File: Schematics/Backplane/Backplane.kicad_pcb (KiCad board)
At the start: 2 copper layers, 69.5 x 98.5 mm, 21 parts, among them J1 Edge Connector (SLOT 1), J2 Edge Connector (SLOT 2), J3 Edge Connector (SLOT 3), J4 Edge Connector (SLOT 4), J5 Edge Connector (SLOT 5), J6 Conn_01x06_Socket

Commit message: New Backplane
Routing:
- net GND1: track 166.7 -> 270.0 mm
- net 24V_A: track 128.8 -> 207.6 mm, vias 1 -> 4
- net BATT_A: track 114.5 -> 179.0 mm, vias 4 -> 6
- net 3.3V_A: track 101.2 -> 157.0 mm, vias 1 -> 5
- net 3.3V_B: track 125.3 -> 176.5 mm, vias 1 -> 4
- net 5.0V_A: track 119.6 -> 164.0 mm, vias 1 -> 4
- net BATT_B: track 162.5 -> 164.9 mm
- net GND2: track 242.5 -> 240.2 mm
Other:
- board text added: "Backplane PCB Rev 1.1 QRET Mar 2025 Abigail Elms Kennan Bays Owen Price"
- board text removed: "Backplane PCB Rev 1.1 QRET Mar 2025 Kennan Bays Owen Price"

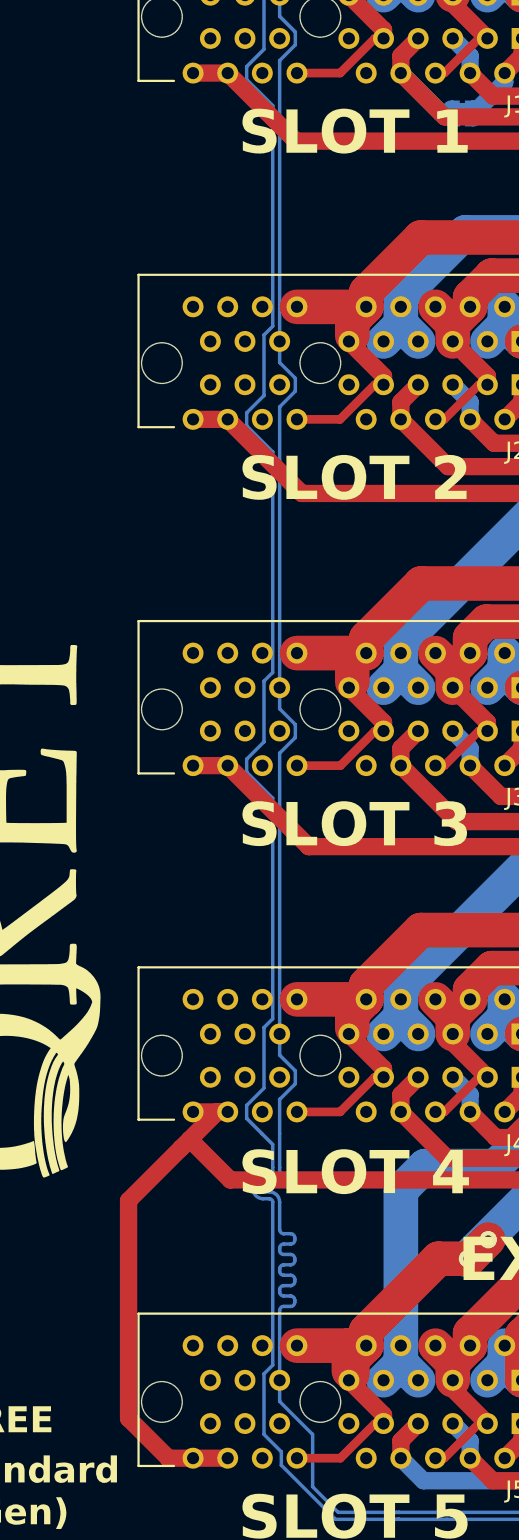
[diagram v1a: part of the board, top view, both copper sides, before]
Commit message: Made Minor Updates
- Update Silk Screen to Reflect 2026 Year
- Connected CAN_P Line to Connectors
- Moved R2 Slightly Away from the Edge
- Fixed DRC Error With J6

Still To Do:
- Name Board
- Update Silkscreen
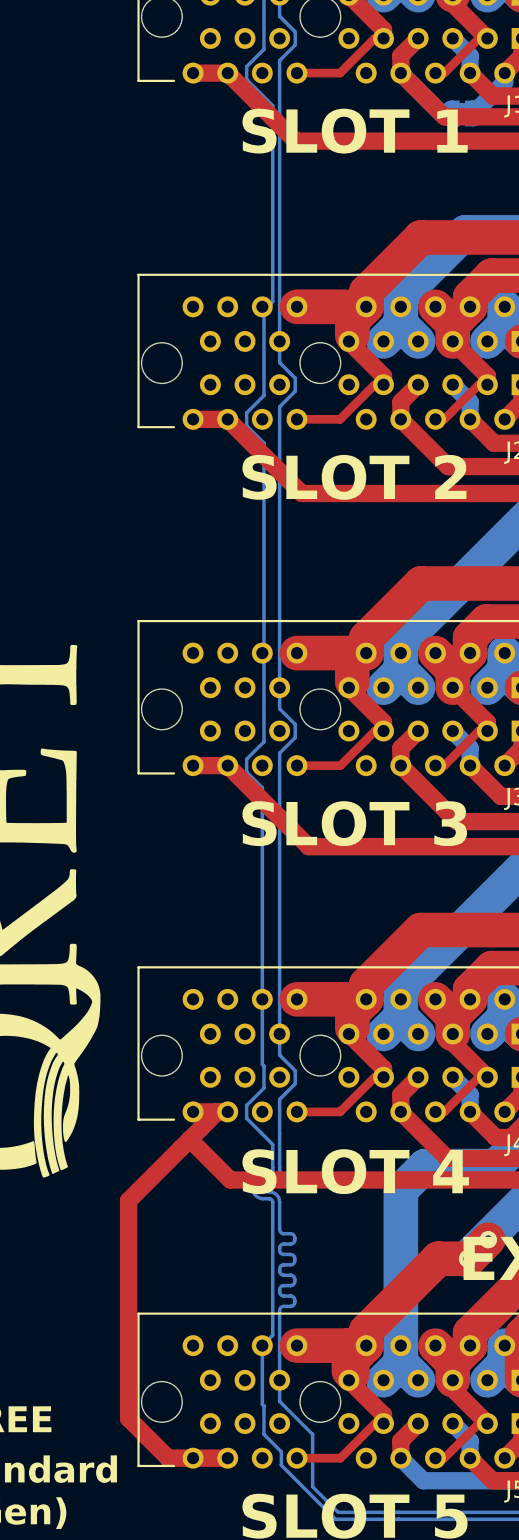
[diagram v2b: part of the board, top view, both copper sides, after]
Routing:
- net CAN_P: track 144.9 -> 144.1 mm
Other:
- board text added: "Backplane PCB Rev 1.2 QRET Mar 2026 Abigail Elms Kennan Bays Owen Price"
- board text removed: "Backplane PCB Rev 1.1 QRET Mar 2025 Abigail Elms Kennan Bays Owen Price"
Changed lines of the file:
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@@
 			(size 3.048 3.048)
 			(drill 3.048)
-			(layers)
+			(layers "*.Mask")
 		)
 		(pad "1" thru_hole circle
@@
 			(pintype "passive")
 		)
-		(model "${KIPRJMOD}/models/430450602.stp"
-			(offset
-				(xyz -3 -4 3.5)
-			)
-			(scale
-				(xyz 1 1 1)
-			)
-			(rotate
-				(xyz -90 0 0)
-			)
-		)
 	)
 	(footprint "Jumper:SolderJumper-2_P1.3mm_Bridged2Bar_RoundedPad1.0x1.5mm"
@@
 		)
 	)
-	(gr_text "Backplane PCB Rev 1.1\nQRET Mar 2025\n\nAbigail Elms\nKennan Bays\nOwen Price"
+	(gr_text "Backplane PCB Rev 1.2\nQRET Mar 2026\n\nAbigail Elms\nKennan Bays\nOwen Price"
 		(at 7.3 29.5 90)
 		(layer "B.SilkS")
@@
 	)
 	(segment
-		(start 29.496 47.79555)
-		(end 30 47.29155)
-		(width 0.2)
-		(layer "B.Cu")
-		(net 30)
-	)
-	(segment
-		(start 28.496 32.29555)
-		(end 29.496 31.29555)
-		(width 0.2)
-		(layer "B.Cu")
-		(net 30)
-	)
-	(segment
-		(start 29.496 3.946001)
-		(end 29.2 3.650001)
+		(start 29.496 91.29555)
+		(end 29.496 89.647714)
 		(width 0.2)
 		(layer "B.Cu")
@@
 	)
 	(segment
-		(start 29.377857 73.926307)
-		(end 28.496 73.04445)
-		(width 0.2)
-		(layer "B.Cu")
-		(net 30)
-	)
-	(segment
-		(start 33.618663 96.2)
-		(end 30.496 93.077337)
-		(width 0.2)
-		(layer "B.Cu")
-		(net 30)
-	)
-	(segment
 		(start 37.274427 96.2)
 		(end 37.160302 96.2)
@@
 	)
 	(segment
-		(start 29.496 11.29555)
-		(end 29.496 3.946001)
+		(start 59.908277 89.363036)
+		(end 60.028277 89.363036)
 		(width 0.2)
 		(layer "B.Cu")
@@
 	)
 	(segment
-		(start 59.908277 89.363036)
-		(end 60.028277 89.363036)
+		(start 30 25.88)
+		(end 30 14.54845)
 		(width 0.2)
 		(layer "B.Cu")
@@
 	)
 	(segment
-		(start 30 87.29155)
-		(end 30 77.883557)
+		(start 66.289909 88.855595)
+		(end 65.934314 88.5)
 		(width 0.2)
 		(layer "B.Cu")
@@
 	)
 	(segment
-		(start 28.496 13.04445)
-		(end 28.496 12.29555)
+		(start 29.496 51.29555)
+		(end 29.496 34.04445)
 		(width 0.2)
 		(layer "B.Cu")
@@
 	)
 	(segment
-		(start 66.289909 88.855595)
-		(end 65.934314 88.5)
+		(start 29.2 3.650001)
+		(end 29.2 2.6)
 		(width 0.2)
 		(layer "B.Cu")
@@
 	)
 	(segment
-		(start 30 27.29155)
-		(end 30 14.54845)
+		(start 28.496 12.29555)
+		(end 29.496 11.29555)
 		(width 0.2)
 		(layer "B.Cu")
@@
 	)
 	(segment
-		(start 29.496 71.29555)
-		(end 29.496 67.79555)
+		(start 30 85.57)
+		(end 30 77.883557)
 		(width 0.2)
 		(layer "B.Cu")
@@
 	)
 	(segment
-		(start 29.496 27.79555)
-		(end 30 27.29155)
+		(start 30 14.54845)
+		(end 28.496 13.04445)
 		(width 0.2)
 		(layer "B.Cu")
@@
 	)
 	(segment
-		(start 30 14.54845)
-		(end 28.496 13.04445)
+		(start 37.160302 96.2)
+		(end 33.618663 96.2)
 		(width 0.2)
 		(layer "B.Cu")
@@
 	)
 	(segment
-		(start 30 74.54845)
-		(end 29.377857 73.926307)
+		(start 28.496 53.04445)
+		(end 28.496 52.29555)
 		(width 0.2)
 		(layer "B.Cu")
@@
 	)
 	(segment
-		(start 29.496 51.29555)
-		(end 29.496 47.79555)
+		(start 30 74.54845)
+		(end 29.377857 73.926307)
 		(width 0.2)
 		(layer "B.Cu")
@@
 	)
 	(segment
-		(start 29.496 67.79555)
-		(end 30 67.29155)
+		(start 29.496 71.29555)
+		(end 29.496 70.024158)
 		(width 0.2)
 		(layer "B.Cu")
@@
 	)
 	(segment
-		(start 29.2 3.650001)
-		(end 29.2 2.6)
+		(start 29.496 3.946001)
+		(end 29.2 3.650001)
+		(width 0.2)
+		(layer "B.Cu")
+		(net 30)
+	)
+	(segment
+		(start 28.496 52.29555)
+		(end 29.496 51.29555)
 		(width 0.2)
 		(layer "B.Cu")
@@
 	)
 	(segment
-		(start 37.160302 96.2)
-		(end 33.618663 96.2)
-		(width 0.2)
-		(layer "B.Cu")
-		(net 30)
-	)
-	(segment
-		(start 29.496 87.79555)
-		(end 30 87.29155)
+		(start 33.618663 96.2)
+		(end 30.496 93.077337)
 		(width 0.2)
 		(layer "B.Cu")
@@
 	)
 	(segment
-		(start 28.496 33.04445)
-		(end 28.496 32.29555)
-		(width 0.2)
-		(layer "B.Cu")
-		(net 30)
-	)
-	(segment
-		(start 66 90)
-		(end 66.289909 89.710091)
+		(start 29.377857 73.926307)
+		(end 28.496 73.04445)
 		(width 0.2)
 		(layer "B.Cu")
@@
 	)
 	(segment
-		(start 61.828277 88.5)
-		(end 62.4 88.5)
+		(start 28.496 72.29555)
+		(end 29.496 71.29555)
 		(width 0.2)
 		(layer "B.Cu")
@@
 	)
 	(segment
-		(start 59.2 88.5)
-		(end 59.428277 88.5)
+		(start 29.4 86.17)
+		(end 30 85.57)
 		(width 0.2)
 		(layer "B.Cu")
@@
 	)
 	(segment
-		(start 28.496 72.29555)
-		(end 29.496 71.29555)
+		(start 28.496 32.29555)
+		(end 29.496 31.29555)
 		(width 0.2)
 		(layer "B.Cu")
@@
 	)
 	(segment
-		(start 28.496 52.29555)
-		(end 29.496 51.29555)
+		(start 28.496 33.04445)
+		(end 28.496 32.29555)
 		(width 0.2)
 		(layer "B.Cu")
@@
 	)
 	(segment
-		(start 37.304773 96.2)
-		(end 37.274427 96.2)
+		(start 66 90)
+		(end 66.289909 89.710091)
 		(width 0.2)
 		(layer "B.Cu")
@@
 	)
 	(segment
-		(start 28.496 12.29555)
-		(end 29.496 11.29555)
+		(start 61.828277 88.5)
+		(end 62.4 88.5)
 		(width 0.2)
 		(layer "B.Cu")
@@
 	)
 	(segment
-		(start 30 47.29155)
-		(end 30 34.54845)
+		(start 30.496 92.29555)
+		(end 29.496 91.29555)
 		(width 0.2)
 		(layer "B.Cu")
@@
 	)
 	(segment
-		(start 60.268277 89.123036)
-		(end 60.268277 88.74)
+		(start 59.2 88.5)
+		(end 59.428277 88.5)
 		(width 0.2)
 		(layer "B.Cu")
@@
 	)
 	(segment
-		(start 29.496 91.29555)
-		(end 29.496 87.79555)
+		(start 37.304773 96.2)
+		(end 37.274427 96.2)
 		(width 0.2)
 		(layer "B.Cu")
@@
 	)
 	(segment
-		(start 30.496 92.29555)
-		(end 29.496 91.29555)
+		(start 29.496 31.29555)
+		(end 29.496 26.384)
 		(width 0.2)
 		(layer "B.Cu")
@@
 	)
 	(segment
-		(start 30 34.54845)
-		(end 28.496 33.04445)
+		(start 60.268277 89.123036)
+		(end 60.268277 88.74)
 		(width 0.2)
 		(layer "B.Cu")
@@
 	)
 	(segment
-		(start 30 54.54845)
-		(end 28.496 53.04445)
+		(start 28.496 73.04445)
+		(end 28.496 72.29555)
 		(width 0.2)
 		(layer "B.Cu")
@@
 	)
 	(segment
-		(start 29.496 31.29555)
-		(end 29.496 27.79555)
+		(start 29.4 89.551714)
+		(end 29.4 86.17)
 		(width 0.2)
 		(layer "B.Cu")
@@
 	)
 	(segment
-		(start 28.496 73.04445)
-		(end 28.496 72.29555)
+		(start 63.899999 87.9)
+		(end 63.899999 87.541553)
 		(width 0.2)
 		(layer "B.Cu")
@@
 	)
 	(segment
-		(start 63.899999 87.9)
-		(end 63.899999 87.541553)
+		(start 59.668277 88.74)
+		(end 59.668277 89.123036)
 		(width 0.2)
 		(layer "B.Cu")
@@
 	)
 	(segment
-		(start 59.668277 88.74)
-		(end 59.668277 89.123036)
+		(start 29.4 53.94845)
+		(end 28.496 53.04445)
 		(width 0.2)
 		(layer "B.Cu")
@@
 	)
 	(segment
-		(start 30 67.29155)
-		(end 30 54.54845)
+		(start 29.496 26.384)
+		(end 30 25.88)
 		(width 0.2)
 		(layer "B.Cu")
@@
 	)
 	(segment
+		(start 29.496 70.024158)
+		(end 29.4 69.928158)
+		(width 0.2)
+		(layer "B.Cu")
+		(net 30)
+	)
+	(segment
+		(start 29.496 34.04445)
+		(end 28.496 33.04445)
+		(width 0.2)
+		(layer "B.Cu")
+		(net 30)
+	)
+	(segment
 		(start 30 75.883557)
 		(end 30 74.54845)
@@
 	)
 	(segment
-		(start 30.496 93.077337)
-		(end 30.496 92.29555)
+		(start 29.496 11.29555)
+		(end 29.496 3.946001)
 		(width 0.2)
 		(layer "B.Cu")
@@
 	)
 	(segment
-		(start 28.496 53.04445)
-		(end 28.496 52.29555)
+		(start 62.699999 88.5)
+		(end 62.499999 88.5)
 		(width 0.2)
 		(layer "B.Cu")
@@
 	)
 	(segment
-		(start 62.699999 88.5)
-		(end 62.499999 88.5)
+		(start 28.496 13.04445)
+		(end 28.496 12.29555)
+		(width 0.2)
+		(layer "B.Cu")
+		(net 30)
+	)
+	(segment
+		(start 30.496 93.077337)
+		(end 30.496 92.29555)
+		(width 0.2)
+		(layer "B.Cu")
+		(net 30)
+	)
+	(segment
+		(start 29.4 69.928158)
+		(end 29.4 53.94845)
 		(width 0.2)
 		(layer "B.Cu")
@@
 		(width 0.2)
 		(layer "B.Cu")
+		(net 30)
+	)
+	(segment
+		(start 29.496 89.647714)
+		(end 29.4 89.551714)
+		(width 0.2)
+		(layer "B.Cu")

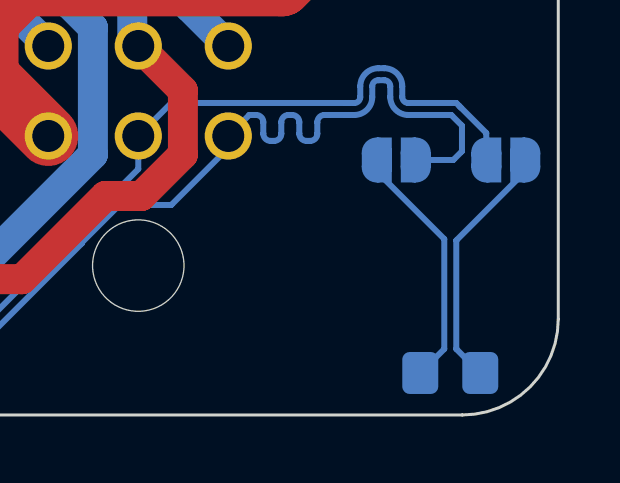
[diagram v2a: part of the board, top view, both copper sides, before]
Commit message: Forgot to save Resistor Move
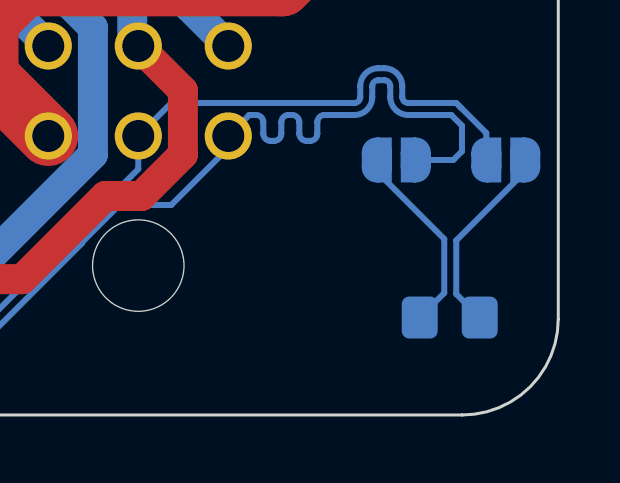
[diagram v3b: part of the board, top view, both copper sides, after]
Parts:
- moved R2 1.85 mm to (65.9, 95.3)
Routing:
- net /TERM_P: track 8.36 -> 6.52 mm
- net /TERM_N: track 8.38 -> 6.55 mm
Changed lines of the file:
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@@
 	(footprint "Resistor_SMD:R_0805_2012Metric_Pad1.20x1.40mm_HandSolder"
 		(layer "B.Cu")
-		(at 65.9 97.1)
+		(at 65.881565 95.251477)
 		(descr "Resistor SMD 0805 (2012 Metric), square (rectangular) end terminal, IPC_7351 nominal with elongated pad for handsoldering. (Body size source: IPC-SM-782 page 72, https://www.pcb-3d.com/wordpress/wp-content/uploads/ipc-sm-782a_amendment_1_and_2.pdf), generated with kicad-footprint-generator")
 		(tags "resistor handsolder")
@@
 	)
 	(segment
-		(start 66.1 92.681337)
-		(end 66.1 96.3)
+		(start 68.4 90.381337)
+		(end 66.1 92.681337)
 		(width 0.2)
 		(layer "B.Cu")
@@
 	)
 	(segment
-		(start 68.4 90)
-		(end 68.4 90.381337)
+		(start 66.1 92.681337)
+		(end 66.1 94.469912)
 		(width 0.2)
 		(layer "B.Cu")
@@
 	)
 	(segment
-		(start 68.4 90.381337)
-		(end 66.1 92.681337)
+		(start 66.1 94.469912)
+		(end 66.9 95.269912)
 		(width 0.2)
 		(layer "B.Cu")
@@
 	)
 	(segment
-		(start 66.1 96.3)
-		(end 66.9 97.1)
+		(start 68.4 90)
+		(end 68.4 90.381337)
 		(width 0.2)
 		(layer "B.Cu")
@@
 	)
 	(segment
-		(start 65.7 92.634314)
-		(end 65.7 96.3)
+		(start 65.7 94.433042)
+		(end 64.881565 95.251477)
 		(width 0.2)
 		(layer "B.Cu")
@@
 	)
 	(segment
-		(start 65.7 96.3)
-		(end 64.9 97.1)
+		(start 63.45 90.384314)
+		(end 65.7 92.634314)
 		(width 0.2)
 		(layer "B.Cu")
@@
 	)
 	(segment
-		(start 63.45 90)
-		(end 63.45 90.384314)
+		(start 65.7 92.634314)
+		(end 65.7 94.433042)
 		(width 0.2)
 		(layer "B.Cu")
@@
 	)
 	(segment
-		(start 63.45 90.384314)
-		(end 65.7 92.634314)
+		(start 63.45 90)
+		(end 63.45 90.384314)
 		(width 0.2)
 		(layer "B.Cu")
